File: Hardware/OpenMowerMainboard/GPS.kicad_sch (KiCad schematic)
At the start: 1 part

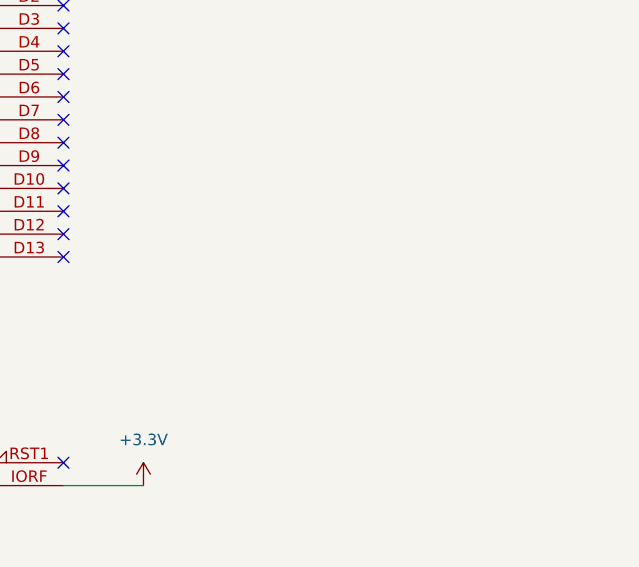
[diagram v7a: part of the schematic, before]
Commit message: BoM data added to kicad - results exported to .xlsx file
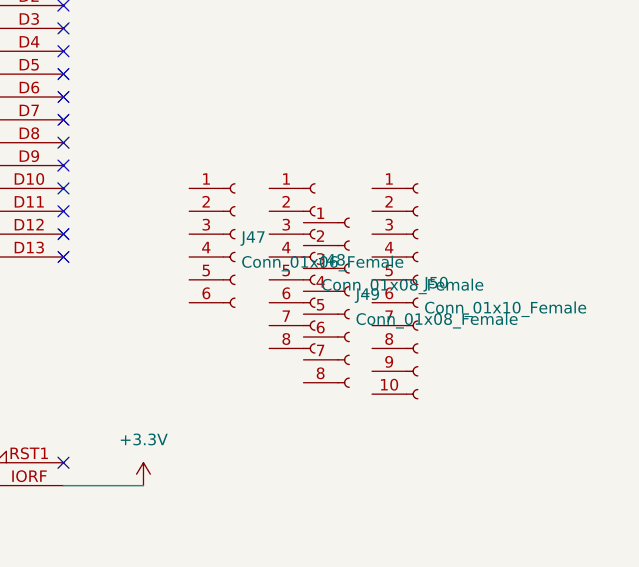
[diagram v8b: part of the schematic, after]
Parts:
- added J47: Conn_01x06_Female, symbol Connector:Conn_01x06_Female
- added J48, J49: Conn_01x08_Female, symbol Connector:Conn_01x08_Female
- added J50: Conn_01x10_Female, symbol Connector:Conn_01x10_Female
- XA1: Config (none) -> do not place
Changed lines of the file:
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@@
     (pin "1")
+  )
+  (symbol (lib_id "Connector:Conn_01x10_Female") (at 227.33 81.28 0) (unit 1)
+    (in_bom yes) (on_board no) (fields_autoplaced)
+    (property "Reference" "J50" (id 0) (at 228.0412 81.6415 0)
+      (effects (font (size 1.27 1.27)) (justify left))
+    )
+    (property "Value" "Conn_01x10_Female" (id 1) (at 228.0412 84.4166 0)
+      (effects (font (size 1.27 1.27)) (justify left))
+    )
+    (property "Footprint" "" (id 2) (at 227.33 81.28 0)
+      (effects (font (size 1.27 1.27)) hide)
+    )
+    (property "Datasheet" "~" (id 3) (at 227.33 81.28 0)
+      (effects (font (size 1.27 1.27)) hide)
+    )
+    (property "LCSC" "C35445" (id 4) (at 227.33 81.28 0)
+      (effects (font (size 1.27 1.27)) hide)
+    )
+    (property "Part Number" "C35445" (id 5) (at 227.33 81.28 0)
+      (effects (font (size 1.27 1.27)) hide)
+    )
+    (property "Stock_PN" "J-TH-1x10-.1F" (id 6) (at 227.33 81.28 0)
+      (effects (font (size 1.27 1.27)) hide)
+    )
+    (pin "1")
+    (pin "10")
+    (pin "2")
+    (pin "3")
+    (pin "4")
+    (pin "5")
+    (pin "6")
+    (pin "7")
+    (pin "8")
+    (pin "9")
   )
   (symbol (lib_id "power:+5V") (at 96.52 98.425 0) (unit 1)
@@
     (pin "1")
   )
+  (symbol (lib_id "Connector:Conn_01x08_Female") (at 219.71 82.55 0) (unit 1)
+    (in_bom yes) (on_board no) (fields_autoplaced)
+    (property "Reference" "J49" (id 0) (at 220.4212 82.9115 0)
+      (effects (font (size 1.27 1.27)) (justify left))
+    )
+    (property "Value" "Conn_01x08_Female" (id 1) (at 220.4212 85.6866 0)
+      (effects (font (size 1.27 1.27)) (justify left))
+    )
+    (property "Footprint" "" (id 2) (at 219.71 82.55 0)
+      (effects (font (size 1.27 1.27)) hide)
+    )
+    (property "Datasheet" "~" (id 3) (at 219.71 82.55 0)
+      (effects (font (size 1.27 1.27)) hide)
+    )
+    (property "LCSC" "C27438" (id 4) (at 219.71 82.55 0)
+      (effects (font (size 1.27 1.27)) hide)
+    )
+    (property "Part Number" "C27438" (id 5) (at 219.71 82.55 0)
+      (effects (font (size 1.27 1.27)) hide)
+    )
+    (property "Stock_PN" "J-TH-1x8-.1F" (id 6) (at 219.71 82.55 0)
+      (effects (font (size 1.27 1.27)) hide)
+    )
+    (pin "1")
+    (pin "2")
+    (pin "3")
+    (pin "4")
+    (pin "5")
+    (pin "6")
+    (pin "7")
+    (pin "8")
+  )
+  (symbol (lib_id "Connector:Conn_01x06_Female") (at 207.01 76.2 0) (unit 1)
+    (in_bom yes) (on_board no) (fields_autoplaced)
+    (property "Reference" "J47" (id 0) (at 207.7212 76.5615 0)
+      (effects (font (size 1.27 1.27)) (justify left))
+    )
+    (property "Value" "Conn_01x06_Female" (id 1) (at 207.7212 79.3366 0)
+      (effects (font (size 1.27 1.27)) (justify left))
+    )
+    (property "Footprint" "" (id 2) (at 207.01 76.2 0)
+      (effects (font (size 1.27 1.27)) hide)
+    )
+    (property "Datasheet" "~" (id 3) (at 207.01 76.2 0)
+      (effects (font (size 1.27 1.27)) hide)
+    )
+    (property "LCSC" "C40877" (id 4) (at 207.01 76.2 0)
+      (effects (font (size 1.27 1.27)) hide)
+    )
+    (property "Part Number" "C40877" (id 5) (at 207.01 76.2 0)
+      (effects (font (size 1.27 1.27)) hide)
+    )
+    (property "Stock_PN" "J-TH-1x6-.1F" (id 6) (at 207.01 76.2 0)
+      (effects (font (size 1.27 1.27)) hide)
+    )
+    (pin "1")
+    (pin "2")
+    (pin "3")
+    (pin "4")
+    (pin "5")
+    (pin "6")
+  )
+  (symbol (lib_id "Connector:Conn_01x08_Female") (at 215.9 78.74 0) (unit 1)
+    (in_bom yes) (on_board no) (fields_autoplaced)
+    (property "Reference" "J48" (id 0) (at 216.6112 79.1015 0)
+      (effects (font (size 1.27 1.27)) (justify left))
+    )
+    (property "Value" "Conn_01x08_Female" (id 1) (at 216.6112 81.8766 0)
+      (effects (font (size 1.27 1.27)) (justify left))
+    )
+    (property "Footprint" "" (id 2) (at 215.9 78.74 0)
+      (effects (font (size 1.27 1.27)) hide)
+    )
+    (property "Datasheet" "~" (id 3) (at 215.9 78.74 0)
+      (effects (font (size 1.27 1.27)) hide)
+    )
+    (property "LCSC" "C27438" (id 4) (at 215.9 78.74 0)
+      (effects (font (size 1.27 1.27)) hide)
+    )
+    (property "Part Number" "C27438" (id 5) (at 215.9 78.74 0)
+      (effects (font (size 1.27 1.27)) hide)
+    )
+    (property "Stock_PN" "J-TH-1x8-.1F" (id 6) (at 215.9 78.74 0)
+      (effects (font (size 1.27 1.27)) hide)
+    )
+    (pin "1")
+    (pin "2")
+    (pin "3")
+    (pin "4")
+    (pin "5")
+    (pin "6")
+    (pin "7")
+    (pin "8")
+  )
   (symbol (lib_id "MyModules:Arduino_Uno_Shield") (at 154.94 77.47 0) (unit 1)
     (in_bom yes) (on_board yes) (fields_autoplaced)
@@
       (effects (font (size 1.524 1.524)) hide)
     )
+    (property "Config" "do not place" (id 4) (at 154.94 77.47 0)
+      (effects (font (size 1.27 1.27)) hide)
+    )
     (pin "3V3")
